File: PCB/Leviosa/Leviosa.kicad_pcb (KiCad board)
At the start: 2 copper layers, 80 x 80 mm, 48 parts, among them J1 2.54mm 1x03 Servo 1, J2 2.54mm 1x03 Servo 1, J3 2.54mm 1x03 Spare, J4 Barrel_Jack, Q3 TIP122, Q4 TIP122, U1 LM324, U2 ATtiny13A-P, U3 TPS1H200AQDGNRQ1, U5 L7805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

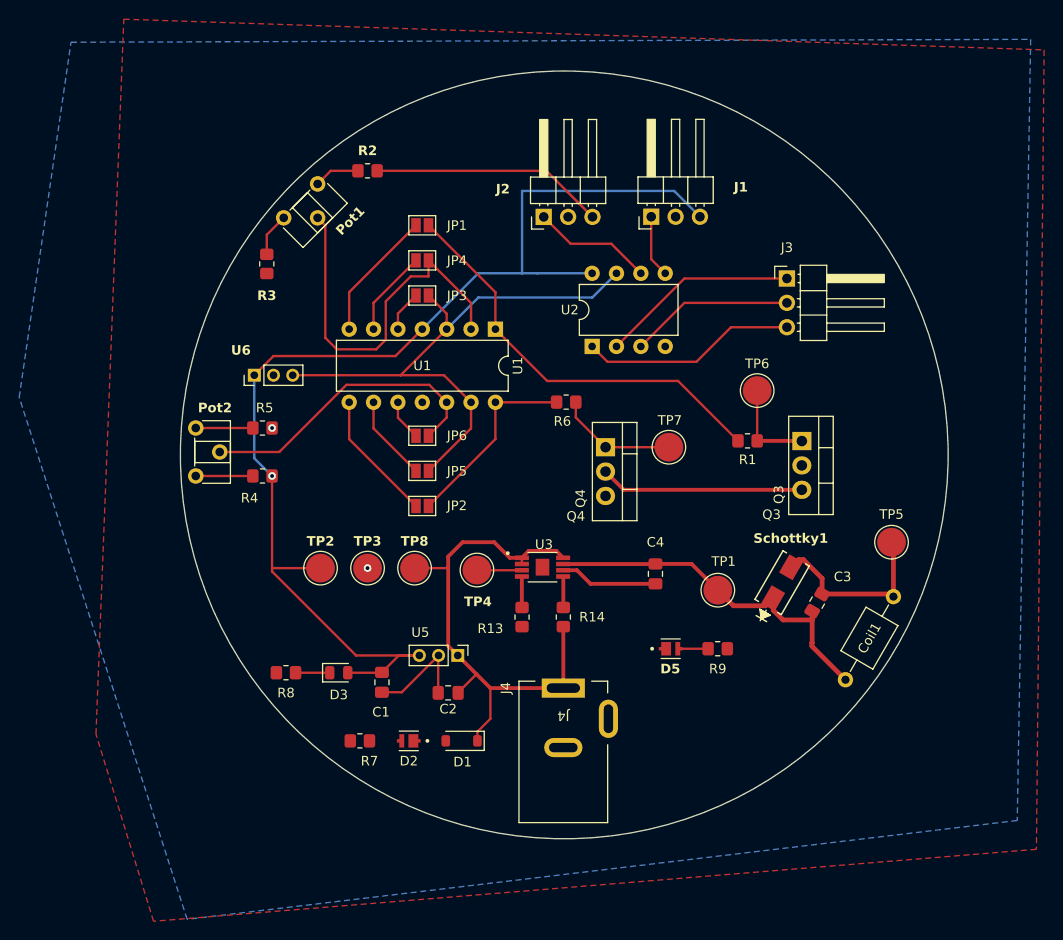
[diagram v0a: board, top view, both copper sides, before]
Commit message: Update silkscreen and indicator diodes
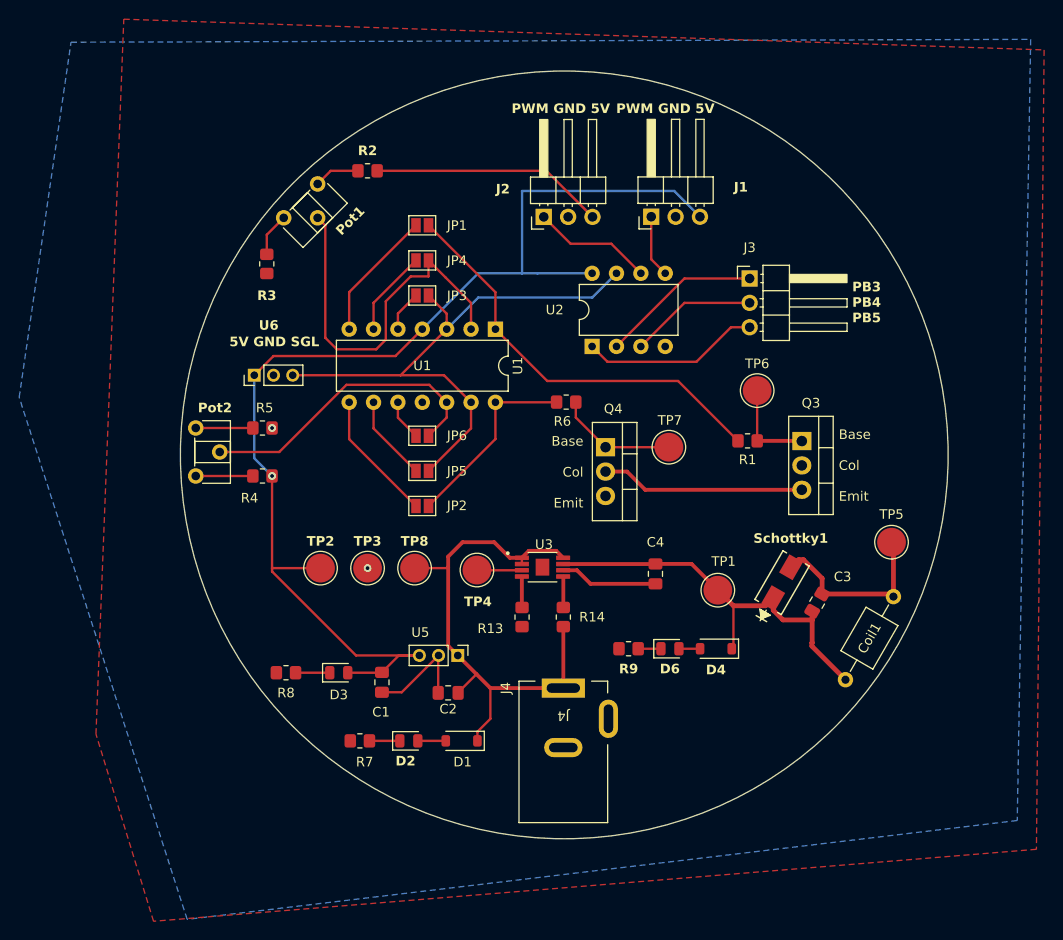
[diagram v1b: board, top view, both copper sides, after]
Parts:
- removed D5: LED, MP-2016-1100-50-70:LED_MP-2016-1100-50-70
- added D4: BZT52C8V2 WD, Diode_SMD:D_SOD-123, F.Cu at (175.8, 140.2)
- added D6: LED, LED_SMD:LED_0805_2012Metric, F.Cu at (171.0, 140.2)
- D2: footprint MP-2016-1100-50-70:LED_MP-2016-1100-50-70 -> LED_SMD:LED_0805_2012Metric
- R9: value 2k4 -> 1kΩ
- moved R9 9.29 mm to (166.7, 140.2)
- moved J3 3.88 mm to (179.3, 101.6)
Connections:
- R9 pad 1: /V_out -> Net-(D6-K)
- R9 pad 2: Net-(D5-PadA) -> GND
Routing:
- net /V_out: track 38.4 -> 43.0 mm
- net /PB4: track 17.1 -> 13.2 mm
- net /PB5: track 22.5 -> 18.6 mm
- net /PB3: track 20.7 -> 16.8 mm
- net Net-(D2-K): track 0.00 -> 3.16 mm
- net Net-(D5-PadA): track 3.04 -> 0.00 mm
- net Net-(D1-A): track 0.00 -> 2.91 mm
- net Net-(D6-K): track 0.00 -> 2.81 mm
- net Net-(D4-A): track 0.00 -> 2.20 mm
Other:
- board text added: "5V GND SGL"
- board text added: "Base Col Emit"
- board text added: "PB3 PB4 PB5"
- board text added: "PWM GND 5V"

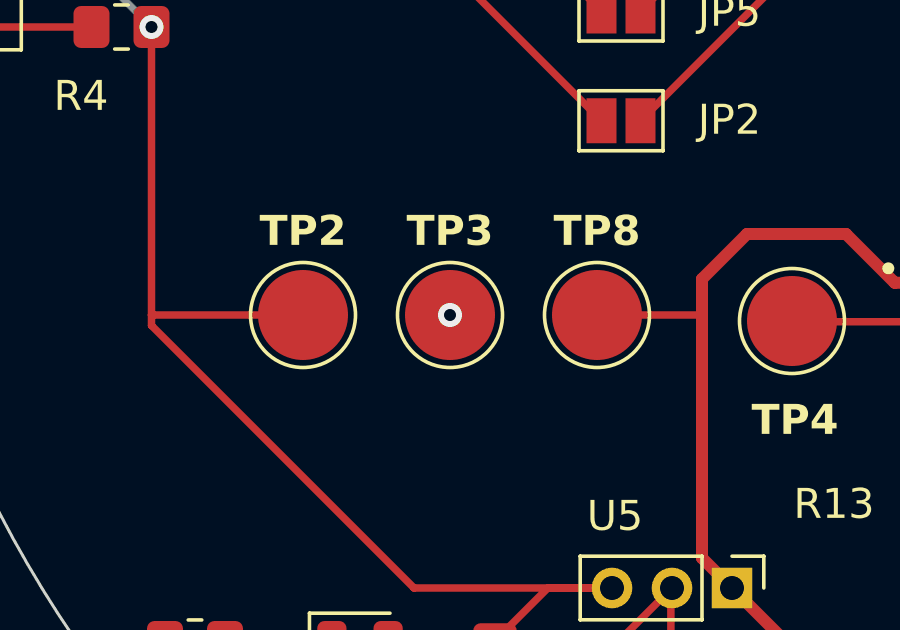
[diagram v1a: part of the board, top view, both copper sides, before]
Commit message: update with 3d models
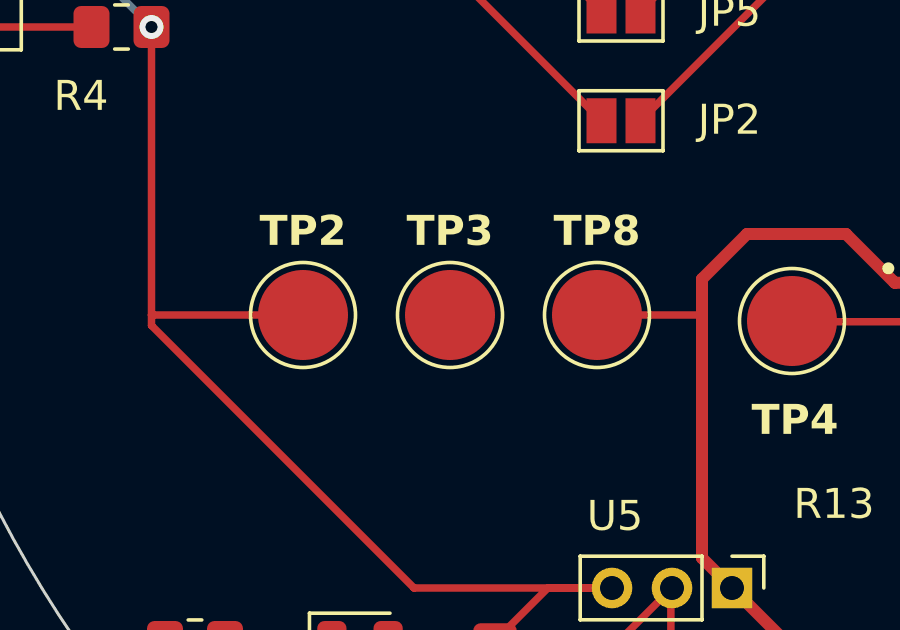
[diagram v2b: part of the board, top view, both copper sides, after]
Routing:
- net GND: vias 2 -> 1
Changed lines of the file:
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@@
 		)
 		(embedded_fonts no)
+		(model "${KIPRJMOD}/Libraries/B230A_13_F.3dshapes/B230A_13_F.step"
+			(offset
+				(xyz 0 0 0)
+			)
+			(scale
+				(xyz 1 1 1)
+			)
+			(rotate
+				(xyz 0 0 0)
+			)
+		)
 	)
 	(footprint "Resistor_SMD:R_0805_2012Metric_Pad1.20x1.40mm_HandSolder"
@@
 		(tags "Potentiometer horizontal ACP CA6-H2,5")
 		(property "Reference" "Pot1"
-			(at 5.116295 0.307969 225)
+			(at 5.116295 0.307969 45)
 			(layer "F.SilkS")
 			(effects
@@
 		)
 		(embedded_fonts no)
-		(model "${KICAD9_3DMODEL_DIR}/Potentiometer_THT.3dshapes/Potentiometer_ACP_CA6-H2,5_Horizontal.step"
+		(model "${KIPRJMOD}/Libraries/3362S-1-103LF.STEP"
 			(offset
-				(xyz 0 0 0)
+				(xyz 1 -2.54 0)
 			)
 			(scale
@@
 			)
 			(rotate
-				(xyz 0 0 0)
+				(xyz -90 -0 90)
 			)
 		)
@@
 			)
 		)
+		(model "${KIPRJMOD}/Libraries/G-014-4.igs"
+			(offset
+				(xyz 7.4 -9.7 -3)
+			)
+			(scale
+				(xyz 1 1 1)
+			)
+			(rotate
+				(xyz -90 -0 90)
+			)
+		)
 	)
 	(footprint "Jumper:SolderJumper-2_P1.3mm_Open_Pad1.0x1.5mm"
@@
 		)
 		(embedded_fonts no)
-		(model "${KICAD9_3DMODEL_DIR}/Potentiometer_THT.3dshapes/Potentiometer_ACP_CA6-H2,5_Horizontal.step"
+		(model "${KIPRJMOD}/Libraries/3362S-1-103LF.STEP"
 			(offset
-				(xyz 0 0 0)
+				(xyz 1 -2.54 0)
 			)
 			(scale
@@
 			)
 			(rotate
-				(xyz 0 0 0)
+				(xyz -90 -0 90)
 			)
 		)
@@
 		(net 3)
 	)
-	(via
-		(at 139.5 131.8)
-		(size 0.8)
-		(drill 0.4)
-		(layers "F.Cu" "B.Cu")
-		(net 3)
-	)

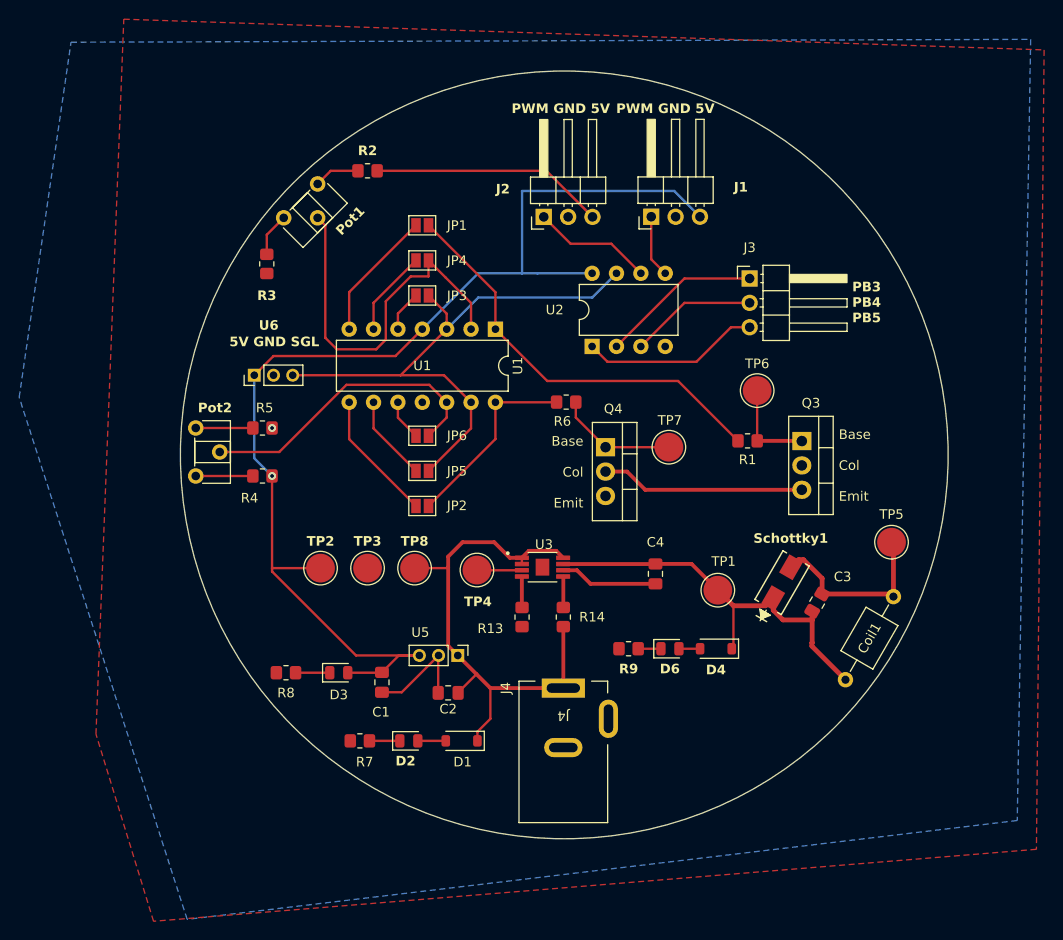
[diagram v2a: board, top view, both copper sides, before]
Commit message: add mounting holes
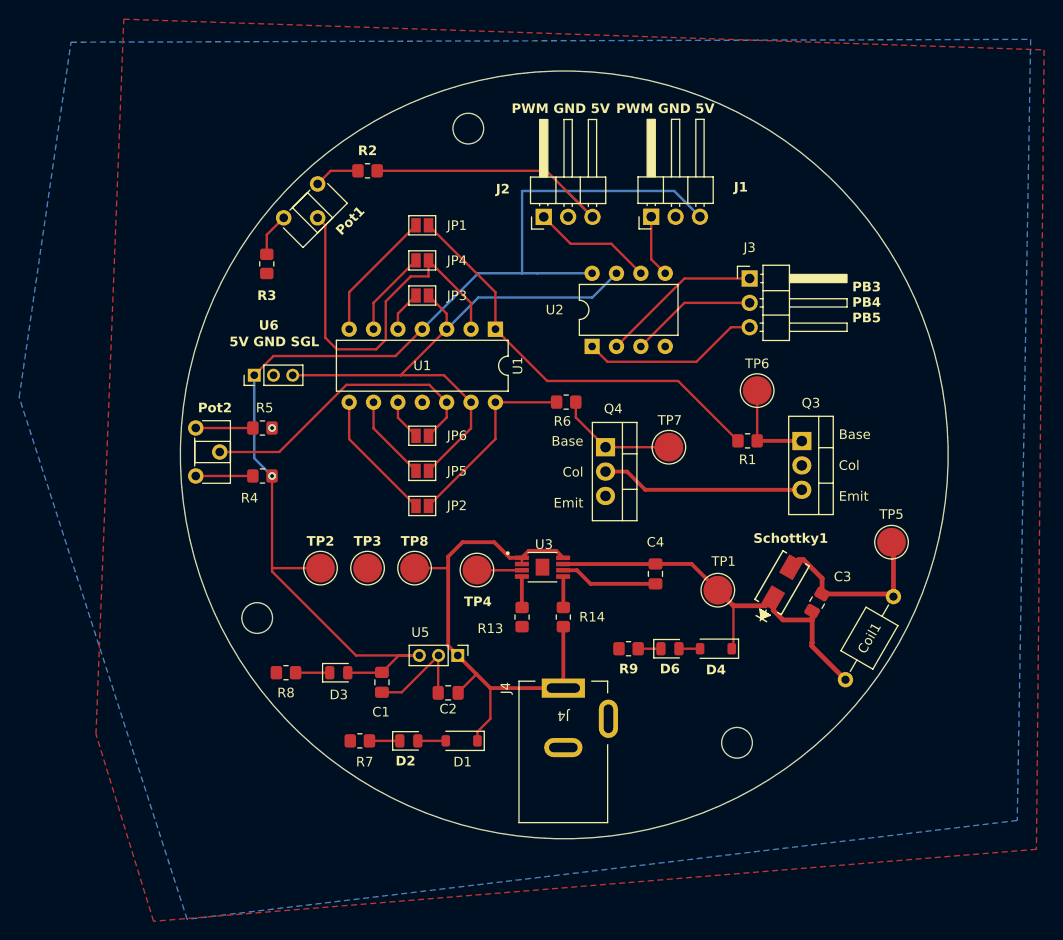
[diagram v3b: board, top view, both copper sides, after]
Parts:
- added H1: MountingHole, MountingHole:MountingHole_3.2mm_M3_ISO7380, F.Cu at (150.0, 86.0)
- added H2: MountingHole, MountingHole:MountingHole_3.2mm_M3_ISO7380, F.Cu at (128.0, 137.0)
- added H3: MountingHole, MountingHole:MountingHole_3.2mm_M3_ISO7380, F.Cu at (178.0, 150.0)

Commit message: added vias
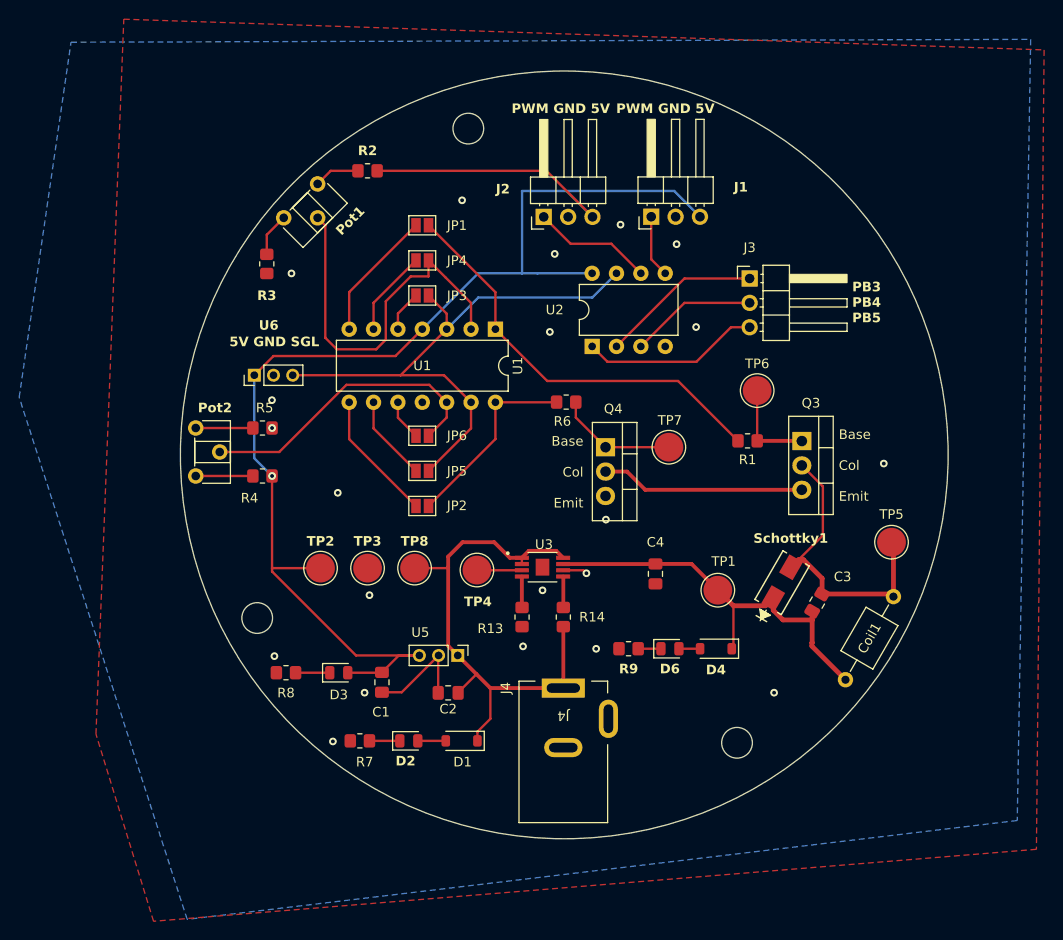
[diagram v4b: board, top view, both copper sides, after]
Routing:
- net /coil_output: track 19.3 -> 32.2 mm
- net GND: track 21.6 -> 14.0 mm, vias 1 -> 21
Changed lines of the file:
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@@
 		(pad "1" smd roundrect
 			(at -2.15 -0.975)
-			(size 1.47 0.48)
+			(size 1.47 0.44)
 			(layers "F.Cu" "F.Mask" "F.Paste")
 			(roundrect_rratio 0.125)
@@
 			(pinfunction "IN")
 			(pintype "input")
-			(solder_mask_margin 0.102)
+			(solder_mask_margin 0.04)
 		)
 		(pad "2" smd roundrect
 			(at -2.15 -0.325)
-			(size 1.47 0.48)
+			(size 1.47 0.44)
 			(layers "F.Cu" "F.Mask" "F.Paste")
 			(roundrect_rratio 0.125)
@@
 			(pinfunction "DIAG_EN")
 			(pintype "input")
-			(solder_mask_margin 0.102)
+			(solder_mask_margin 0.04)
 		)
 		(pad "3" smd roundrect
 			(at -2.15 0.325)
-			(size 1.47 0.48)
+			(size 1.47 0.44)
 			(layers "F.Cu" "F.Mask" "F.Paste")
 			(roundrect_rratio 0.125)
@@
 			(pinfunction "~{FAULT}")
 			(pintype "output")
-			(solder_mask_margin 0.102)
+			(solder_mask_margin 0.04)
 		)
 		(pad "4" smd roundrect
 			(at -2.15 0.975)
-			(size 1.47 0.48)
+			(size 1.47 0.44)
 			(layers "F.Cu" "F.Mask" "F.Paste")
 			(roundrect_rratio 0.125)
@@
 			(pinfunction "CL")
 			(pintype "output")
-			(solder_mask_margin 0.102)
+			(solder_mask_margin 0.04)
 		)
 		(pad "5" smd roundrect
 			(at 2.15 0.975)
-			(size 1.47 0.48)
+			(size 1.47 0.44)
 			(layers "F.Cu" "F.Mask" "F.Paste")
 			(roundrect_rratio 0.125)
@@
 			(pinfunction "DELAY")
 			(pintype "bidirectional")
-			(solder_mask_margin 0.102)
+			(solder_mask_margin 0.04)
 		)
 		(pad "6" smd roundrect
 			(at 2.15 0.325)
-			(size 1.47 0.48)
+			(size 1.47 0.44)
 			(layers "F.Cu" "F.Mask" "F.Paste")
 			(roundrect_rratio 0.125)
@@
 			(pinfunction "GND")
 			(pintype "power_in")
-			(solder_mask_margin 0.102)
+			(solder_mask_margin 0.04)
 		)
 		(pad "7" smd roundrect
 			(at 2.15 -0.325)
-			(size 1.47 0.48)
+			(size 1.47 0.44)
 			(layers "F.Cu" "F.Mask" "F.Paste")
 			(roundrect_rratio 0.125)
@@
 			(pinfunction "OUT")
 			(pintype "output")
-			(solder_mask_margin 0.102)
+			(solder_mask_margin 0.04)
 		)
 		(pad "8" smd roundrect
 			(at 2.15 -0.975)
-			(size 1.47 0.48)
+			(size 1.47 0.44)
 			(layers "F.Cu" "F.Mask" "F.Paste")
 			(roundrect_rratio 0.125)
@@
 			(pinfunction "VS")
 			(pintype "power_in")
-			(solder_mask_margin 0.102)
+			(solder_mask_margin 0.04)
 		)
 		(pad "9" smd rect
@@
 			(pinfunction "EP")
 			(pintype "bidirectional")
-			(solder_mask_margin 0.102)
+			(solder_mask_margin 0.04)
 		)
 		(embedded_fonts no)
@@
 	)
 	(segment
-		(start 161.325 132.025)
-		(end 162.7375 133.4375)
-		(width 0.4)
-		(layer "F.Cu")
-		(net 3)
-	)
-	(segment
-		(start 159.88 132.025)
-		(end 161.325 132.025)
-		(width 0.4)
-		(layer "F.Cu")
-		(net 3)
-	)
-	(segment
 		(start 146.8625 144.8)
 		(end 146.8625 140.9375)
@@
 	)
 	(segment
+		(start 161.997 132.025)
+		(end 159.88 132.025)
+		(width 0.25)
+		(layer "F.Cu")
+		(net 3)
+	)
+	(segment
 		(start 143.0625 144.7375)
 		(end 146.9 140.9)
@@
 	)
 	(segment
-		(start 162.7375 133.4375)
-		(end 169.5 133.4375)
-		(width 0.4)
-		(layer "F.Cu")
+		(start 162.306 132.334)
+		(end 161.997 132.025)
+		(width 0.25)
+		(layer "F.Cu")
+		(net 3)
+	)
+	(via
+		(at 135.89 149.86)
+		(size 0.8)
+		(drill 0.4)
+		(layers "F.Cu" "B.Cu")
+		(free yes)
+		(net 3)
+	)
+	(via
+		(at 164.338 126.746)
+		(size 0.8)
+		(drill 0.4)
+		(layers "F.Cu" "B.Cu")
+		(free yes)
+		(net 3)
+	)
+	(via
+		(at 131.572 101.092)
+		(size 0.8)
+		(drill 0.4)
+		(layers "F.Cu" "B.Cu")
+		(free yes)
+		(net 3)
+	)
+	(via
+		(at 129.54 114.3)
+		(size 0.8)
+		(drill 0.4)
+		(layers "F.Cu" "B.Cu")
+		(free yes)
+		(net 3)
+	)
+	(via
+		(at 157.734 134.112)
+		(size 0.8)
+		(drill 0.4)
+		(layers "F.Cu" "B.Cu")
+		(free yes)
+		(net 3)
+	)
+	(via
+		(at 139.7 134.62)
+		(size 0.8)
+		(drill 0.4)
+		(layers "F.Cu" "B.Cu")
+		(free yes)
+		(net 3)
+	)
+	(via
+		(at 193.294 120.904)
+		(size 0.8)
+		(drill 0.4)
+		(layers "F.Cu" "B.Cu")
+		(free yes)
+		(net 3)
+	)
+	(via
+		(at 165.862 96.012)
+		(size 0.8)
+		(drill 0.4)
+		(layers "F.Cu" "B.Cu")
+		(free yes)
+		(net 3)
+	)
+	(via
+		(at 139.192 144.78)
+		(size 0.8)
+		(drill 0.4)
+		(layers "F.Cu" "B.Cu")
+		(free yes)
 		(net 3)
 	)
@@
 		(layers "F.Cu" "B.Cu")
 		(net 3)
+	)
+	(via
+		(at 149.352 93.472)
+		(size 0.8)
+		(drill 0.4)
+		(layers "F.Cu" "B.Cu")
+		(free yes)
+		(net 3)
+	)
+	(via
+		(at 159.004 99.06)
+		(size 0.8)
+		(drill 0.4)
+		(layers "F.Cu" "B.Cu")
+		(free yes)
+		(net 3)
+	)
+	(via
+		(at 162.306 132.334)
+		(size 0.8)
+		(drill 0.4)
+		(layers "F.Cu" "B.Cu")
+		(free yes)
+		(net 3)
+	)
+	(via
+		(at 158.496 107.188)
+		(size 0.8)
+		(drill 0.4)
+		(layers "F.Cu" "B.Cu")
+		(free yes)
+		(net 3)
+	)
+	(via
+		(at 155.702 139.954)
+		(size 0.8)
+		(drill 0.4)
+		(layers "F.Cu" "B.Cu")
+		(free yes)
+		(net 3)
+	)
+	(via
+		(at 181.864 144.78)
+		(size 0.8)
+		(drill 0.4)
+		(layers "F.Cu" "B.Cu")
+		(free yes)
+		(net 3)
+	)
+	(via
+		(at 163.322 140.208)
+		(size 0.8)
+		(drill 0.4)
+		(layers "F.Cu" "B.Cu")
+		(free yes)
+		(net 3)
+	)
+	(via
+		(at 129.794 140.97)
+		(size 0.8)
+		(drill 0.4)
+		(layers "F.Cu" "B.Cu")
+		(free yes)
+		(net 3)
+	)
+	(via
+		(at 173.736 106.68)
+		(size 0.8)
+		(drill 0.4)
+		(layers "F.Cu" "B.Cu")
+		(free yes)
+		(net 3)
+	)
+	(via
+		(at 171.704 98.044)
+		(size 0.8)
+		(drill 0.4)
+		(layers "F.Cu" "B.Cu")
+		(free yes)
+		(net 3)
+	)
+	(via
+		(at 136.398 123.952)
+		(size 0.8)
+		(drill 0.4)
+		(layers "F.Cu" "B.Cu")
+		(free yes)
+		(net 3)
+	)
+	(segment
+		(start 186.944 128.396041)
+		(end 183.6286 131.711441)
+		(width 0.25)
+		(layer "F.Cu")
+		(net 4)
 	)
 	(segment
@@
 	)
 	(segment
+		(start 186.944 123.289)
+		(end 186.944 128.396041)
+		(width 0.25)
+		(layer "F.Cu")
+		(net 4)
+	)
+	(segment
 		(start 186.86875 132.869156)
 		(end 184.912953 130.913359)
@@
 		(layer "F.Cu")
 		(net 4)
+	)
+	(segment
+		(start 184.755 121.1)
+		(end 186.944 123.289)
+		(width 0.25)
+		(layer "F.Cu")
+		(net 4)

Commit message: added text
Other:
- board text added: "12V"
- board text added: "5V"
- board text added: "Coil"
- board text added: "GND"
- board text added: "V_out"
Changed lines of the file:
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@@
+		)
+	)
+	(gr_text "Coil\n"
+		(at 191.77 133.096 0)
+		(layer "F.SilkS")
+		(effects
+			(font
+				(size 1.5 1.5)
+				(thickness 0.3)
+				(bold yes)
+			)
+			(justify left bottom)
 		)
 	)
@@
 				(size 1 1)
 				(thickness 0.2)
+				(bold yes)
+			)
+			(justify left bottom)
+		)
+	)
+	(gr_text "12V\n"
+		(at 142.24 136.144 0)
+		(layer "F.SilkS")
+		(effects
+			(font
+				(size 1.5 1.5)
+				(thickness 0.3)
 				(bold yes)
 			)
@@
 		)
 	)
+	(gr_text "V_out\n"
+		(at 168.656 137.414 0)
+		(layer "F.SilkS")
+		(effects
+			(font
+				(size 1.5 1.5)
+				(thickness 0.3)
+				(bold yes)
+			)
+			(justify left bottom)
+		)
+	)
+	(gr_text "5V"
+		(at 133.096 135.89 0)
+		(layer "F.SilkS")
+		(effects
+			(font
+				(size 1.5 1.5)
+				(thickness 0.3)
+				(bold yes)
+			)
+			(justify left bottom)
+		)
+	)
 	(gr_text "Base\n\nCol\n\nEmit"
 		(at 162 121.8 0)
@@
 		)
 	)
+	(gr_text "GND\n"
+		(at 136.906 136.144 0)
+		(layer "F.SilkS")
+		(effects
+			(font
+				(size 1.5 1.5)
+				(thickness 0.3)
+				(bold yes)
+			)
+			(justify left bottom)
+		)
+	)
